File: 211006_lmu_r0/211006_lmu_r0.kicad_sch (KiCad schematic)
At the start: 16 parts, among them J1 Conn_02x03_Odd_Even, J14 Conn_01x02, J15 Conn_01x02, J16 Conn_01x02, J17 Conn_01x02, J18 Conn_01x02, J19 Conn_01x02, J2 Conn_02x03_Odd_Even, J20 Conn_01x02, J21 Conn_01x02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

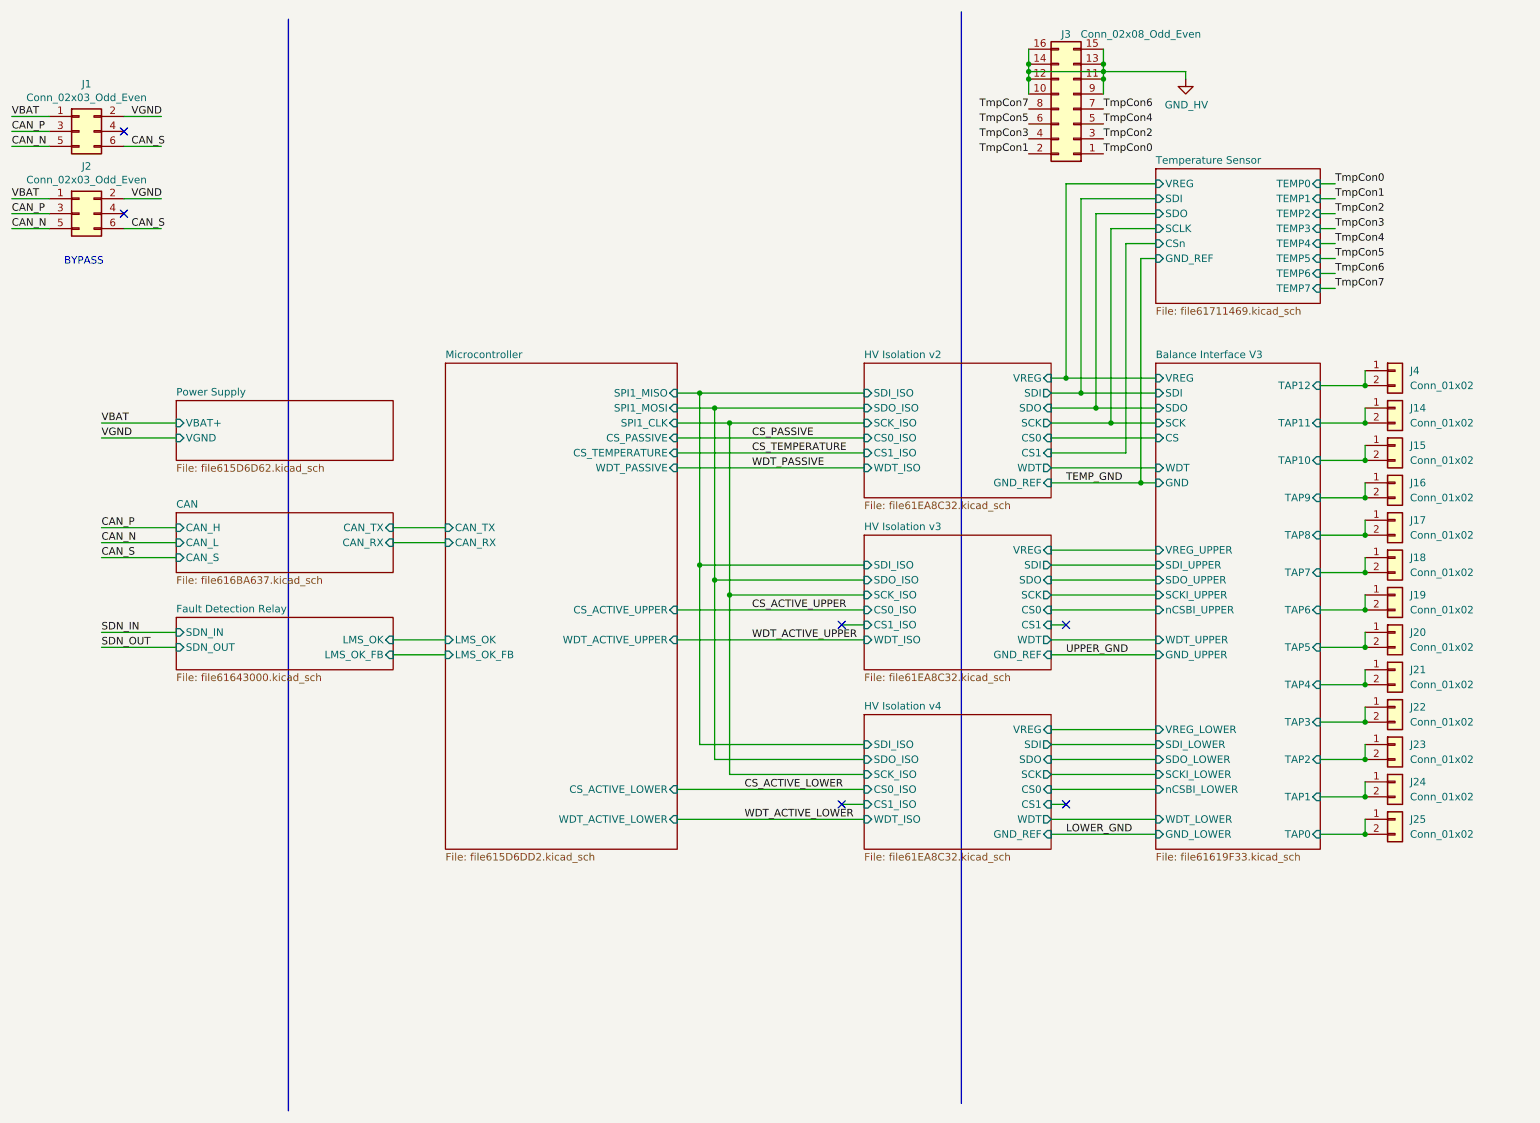
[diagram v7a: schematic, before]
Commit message: updated pcb still need to find j11
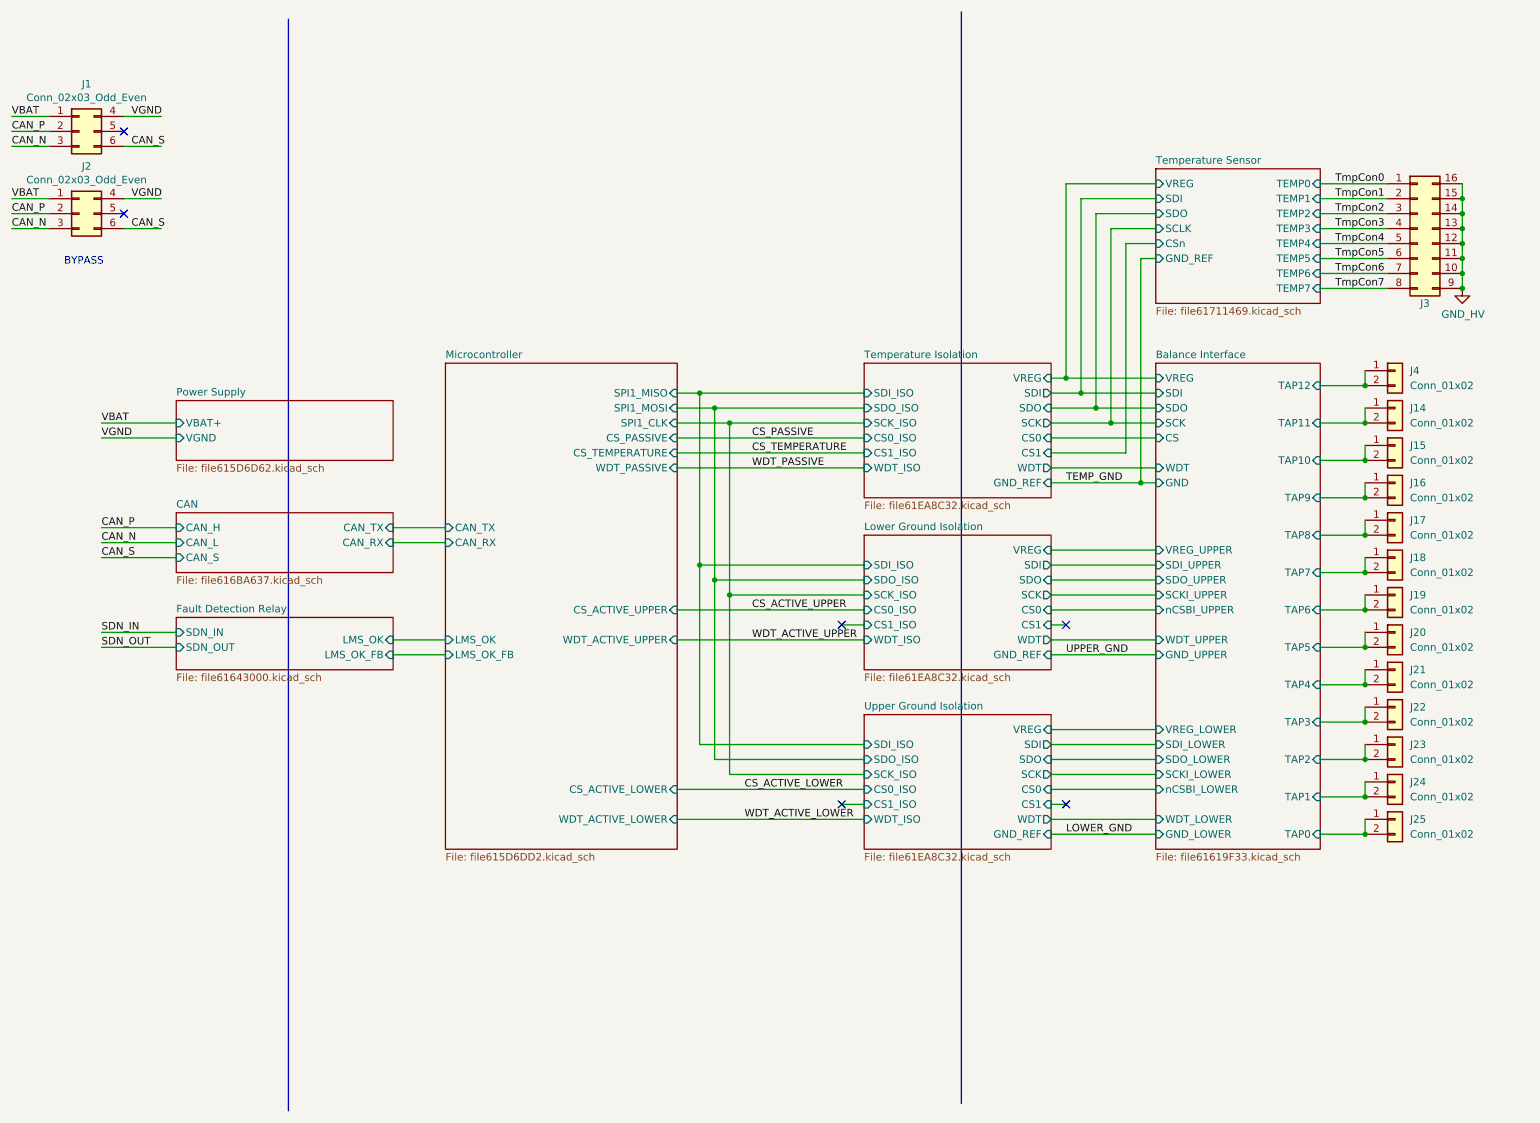
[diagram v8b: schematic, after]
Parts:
- J1, J2: symbol Connector_Generic:Conn_02x03_Odd_Even -> Connector_Generic:Conn_02x03_Top_Bottom
- J3: symbol Connector_Generic:Conn_02x08_Odd_Even -> Connector_Generic:Conn_02x08_Counter_Clockwise
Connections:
- net CAN_N: now also J1.3 (Pin_3), J2.3 (Pin_3); no longer J1.5 (Pin_5), J2.5 (Pin_5)
- net CAN_P: now also J1.2 (Pin_2), J2.2 (Pin_2); no longer J1.3 (Pin_3), J2.3 (Pin_3)
- net VGND: now also J1.4 (Pin_4), J2.4 (Pin_4); no longer J1.2 (Pin_2), J2.2 (Pin_2)
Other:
- sheet Balance Interface V3 renamed Balance Interface
- sheet HV Isolation v2 renamed Temperature Isolation
- sheet HV Isolation v3 renamed Lower Ground Isolation
- sheet HV Isolation v4 renamed Upper Ground Isolation
- moved on the sheet: J3
